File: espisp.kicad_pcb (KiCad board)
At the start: 2 copper layers, 17 x 27 mm, 25 parts, among them P1 FTDI_BASIC, Q1 2N7002, Q2 2N7002, SW1 RESET, U1 ESP-12, U2 XC6206

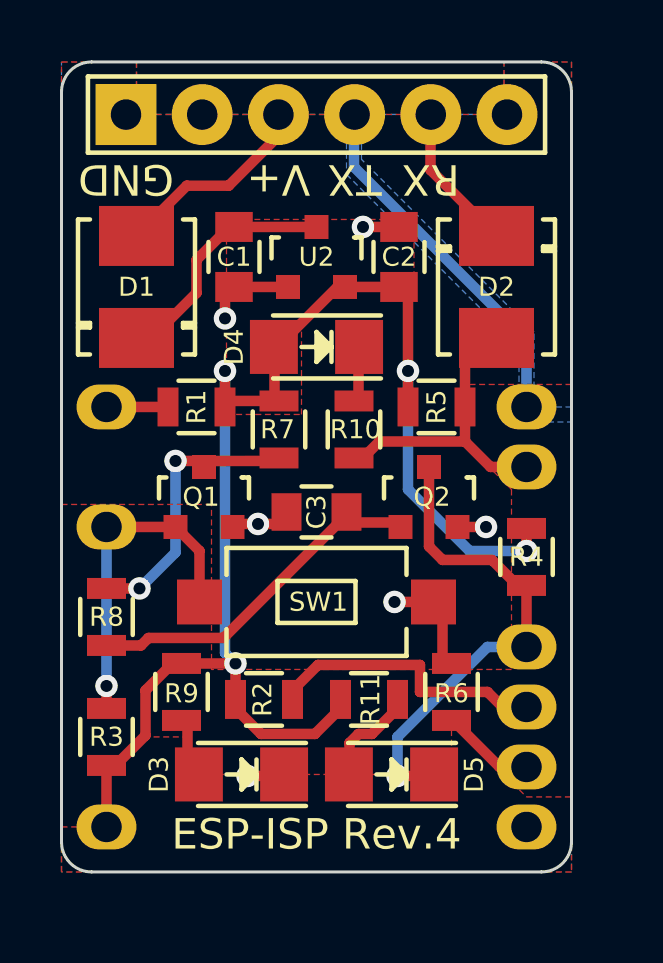
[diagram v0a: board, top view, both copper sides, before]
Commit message: Placement tweaking and full reroute. (Rev. 5)
* Moved the power LED near the power components.
* All polarized components have the same orientation.
* Extended the rim so the board can be held down easier.
* Moved vias out from under components to make them easier to place.
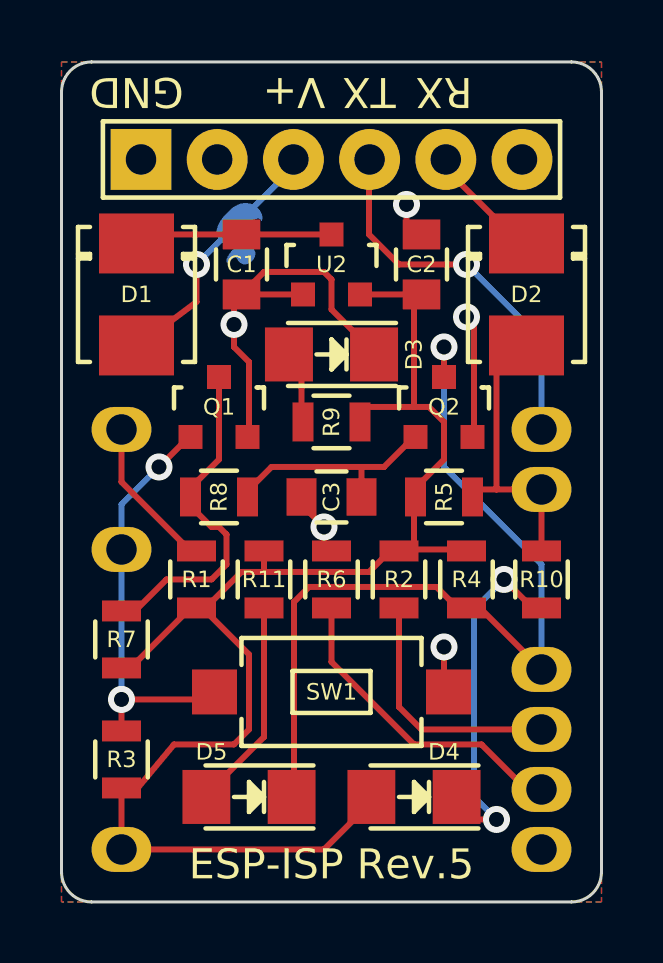
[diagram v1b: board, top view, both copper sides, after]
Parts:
- added G***: LOGO, my_footprints:Ferret_Logo_0.1in, B.Cu at (55.5, 41.2)
- added G***: LOGO, my_footprints:OSHW_Logo_0.1in, B.Cu at (58.5, 41.0)
- added G***: DUCK, my_footprints:DUCK, B.Cu at (49.0, 29.8)
- moved D4 15.3 mm to (54.8, 48.5)
- moved D3 14.3 mm to (52.0, 33.8)
- moved R9 10.3 mm to (52.0, 36.0), turned to 0 degrees
- moved R7 8.75 mm to (45.0, 43.2), turned to 90 degrees
- moved R10 8.00 mm to (59.0, 41.2), turned to 90 degrees
- moved R2 6.02 mm to (54.2, 41.2), turned to 270 degrees
- moved R1 5.75 mm to (47.5, 41.2), turned to 90 degrees
- moved R6 5.48 mm to (52.0, 41.2)
- moved R8 5.48 mm to (48.2, 38.5), turned to 0 degrees
- moved R11 5.32 mm to (49.8, 41.2), turned to 270 degrees
- moved D5 4.81 mm to (49.2, 48.5)
- moved Q1 3.04 mm to (48.2, 35.5)
- moved Q2 3.04 mm to (55.8, 35.5)
- moved SW1 3.04 mm to (52.0, 45.0)
- moved R5 3.01 mm to (55.8, 38.5)
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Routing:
- net /GPIO0: track 16.5 -> 28.9 mm
- net GND: track 12.0 -> 21.8 mm, vias 6 -> 5
- net Net-(D4-Pad1): track 1.80 -> 11.4 mm, vias 0 -> 2
- net /GPIO15: track 3.09 -> 10.0 mm
- net Net-(C3-Pad1): track 11.5 -> 7.47 mm
- net Net-(D5-Pad2): track 3.18 -> 6.72 mm
- net /VIN_5V: track 5.36 -> 8.35 mm, vias 0 -> 1
- net /RESET: track 2.10 -> 4.93 mm
- net /CH_PD: track 11.2 -> 13.7 mm, vias 1 -> 2
- net Net-(Q1-Pad3): track 9.25 -> 11.1 mm, vias 2 -> 0
- net Net-(C1-Pad1): track 7.68 -> 6.50 mm
- net /RXD: track 9.98 -> 9.00 mm
- net /GPIO2: track 9.19 -> 8.31 mm
- net /RXD_5V: track 4.21 -> 3.54 mm
- net +3V3: track 47.5 -> 46.9 mm, vias 4 -> 0
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- removed copper zone on B.Cu, net (none)
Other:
- board size 17 x 27 mm -> 18 x 28 mm
- net class Default: clearance 0.175 -> 0.2; trace_width 0.35 -> 0.2; via_dia 0.75 -> 0.9; via_drill 0.4 -> 0.5
- rule trace_clearance: 0.175 -> 0.2
- rule trace_min: 0.175 -> 0.2
- rule via_min_drill: 0.4 -> 0.5
- rule via_min_size: 0.75 -> 0.7
- board text added: "ESP-ISP Rev.5"
- board text added: "SPMC"
- board text added: "WiFi Antenna"
- board text removed: "ESP-ISP Rev.4"
